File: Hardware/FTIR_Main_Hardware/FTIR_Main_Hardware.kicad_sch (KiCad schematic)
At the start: 78 parts, among them J1 RJ45_LED_Shielded, Q1 IRF7606PBF, Q2 BSS138, Q3 IRF7606PBF, Q4 BSS138, Q5 IRF7606PBF, Q6 BSS138, U1 Opamp_Dual, U2 TMC2208, U3 OKI, U6 Peensy4.1_DEV-16771, U7 OKI

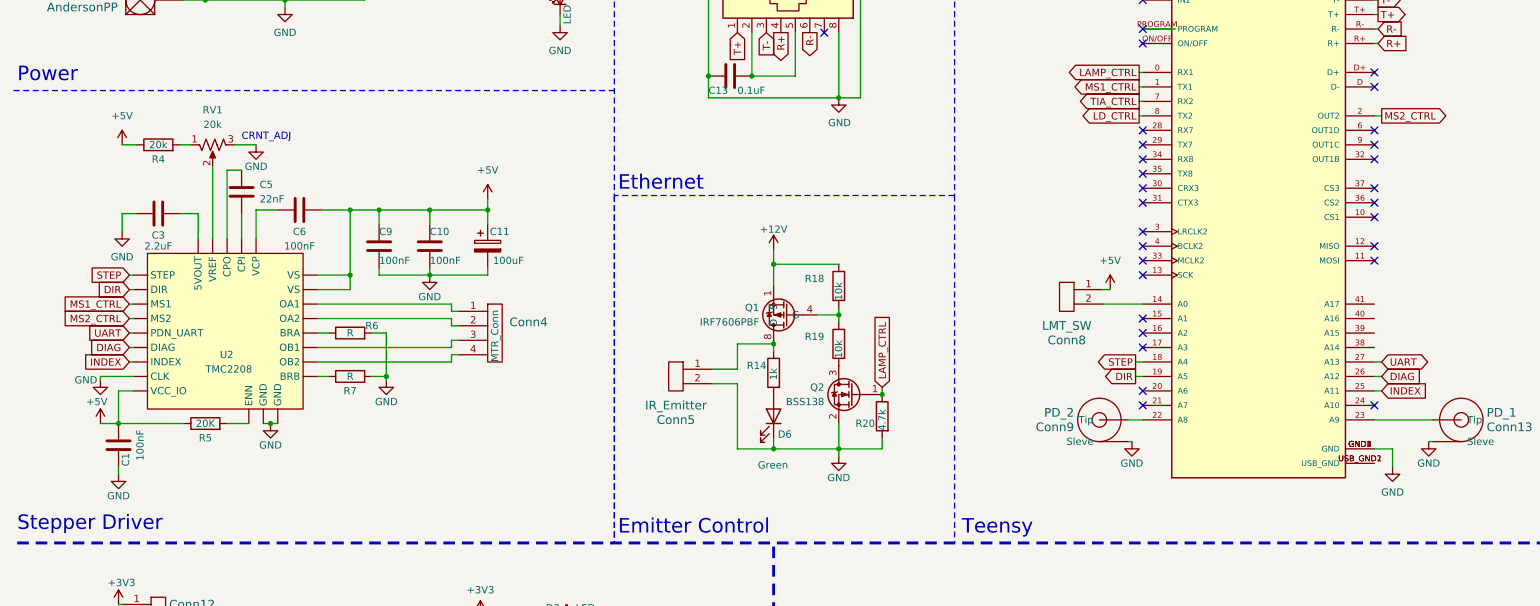
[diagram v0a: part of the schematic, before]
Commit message: Added breakouts
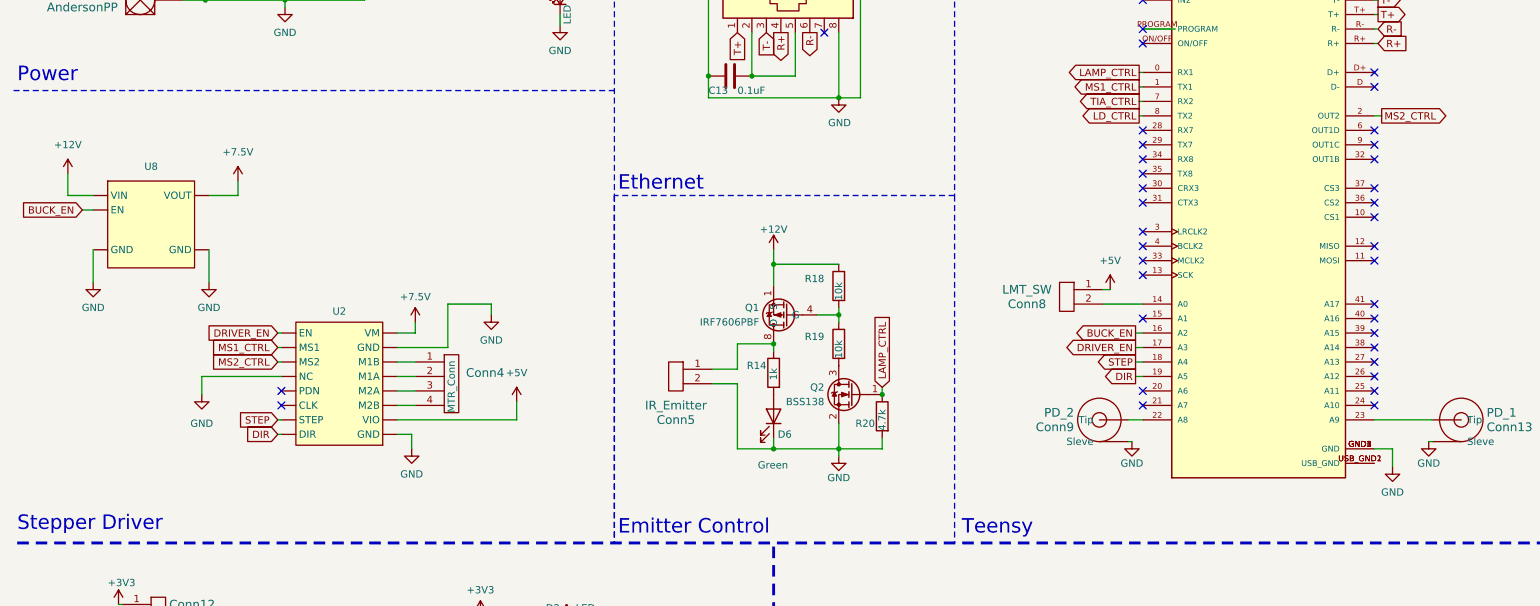
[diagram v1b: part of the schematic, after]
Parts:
- removed C1, C10, C6, C9: 100nF, symbol Device:C
- removed C11: 100uF, symbol Device:C_Polarized
- removed C3: 2.2uF, symbol Device:C
- removed C5: 22nF, symbol Device:C
- removed R4: 20k, symbol Device:R
- removed R5: 20K, symbol Device:R
- removed R6, R7: R, symbol Device:R
- removed RV1: 20k, symbol Device:R_Potentiometer_US
- removed U2: TMC2208, symbol MRDT_Devices:TMC2208
- added U2: ~, symbol Stepper_Driver_Headers:TMC2208_Breakout
- added U8: ~, symbol Stepper_Driver_Headers:Pololu_7v5_Stepdown
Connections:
- net +12V: now also U8. (VOUT)
- net +5V: now also U2. (VM)
- net DIR: now also U2. (VM)
- net GND: now also U2. (VM), U8. (VOUT)
- net MS1_CTRL: now also U2. (VM)
- net MS2_CTRL: now also U2. (VM)
- net STEP: now also U2. (VM)
- net at Conn4.1: now also U2. (VM)
- net at Conn4.2: now also U2. (VM)
- net at Conn4.3: now also U2. (VM)
- net at Conn4.4: now also U2. (VM)
- net BUCK_EN: now reaches U6.16 (A2)
- net BUCK_EN: now also U8. (VOUT)
- net DRIVER_EN: now reaches U6.17 (A3)
- net DRIVER_EN: now also U2. (VM)
- net DIAG: no longer names the net of U6.26 (A12)
- net INDEX: no longer names the net of U6.25 (A11)
- net UART: no longer names the net of U6.27 (A13)
- new net +7.5V: U2. (VM), U8. (VOUT)
- no-connect marks 37 -> 44
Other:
- note removed: "CRNT_ADJ"
- moved on the sheet: Conn4

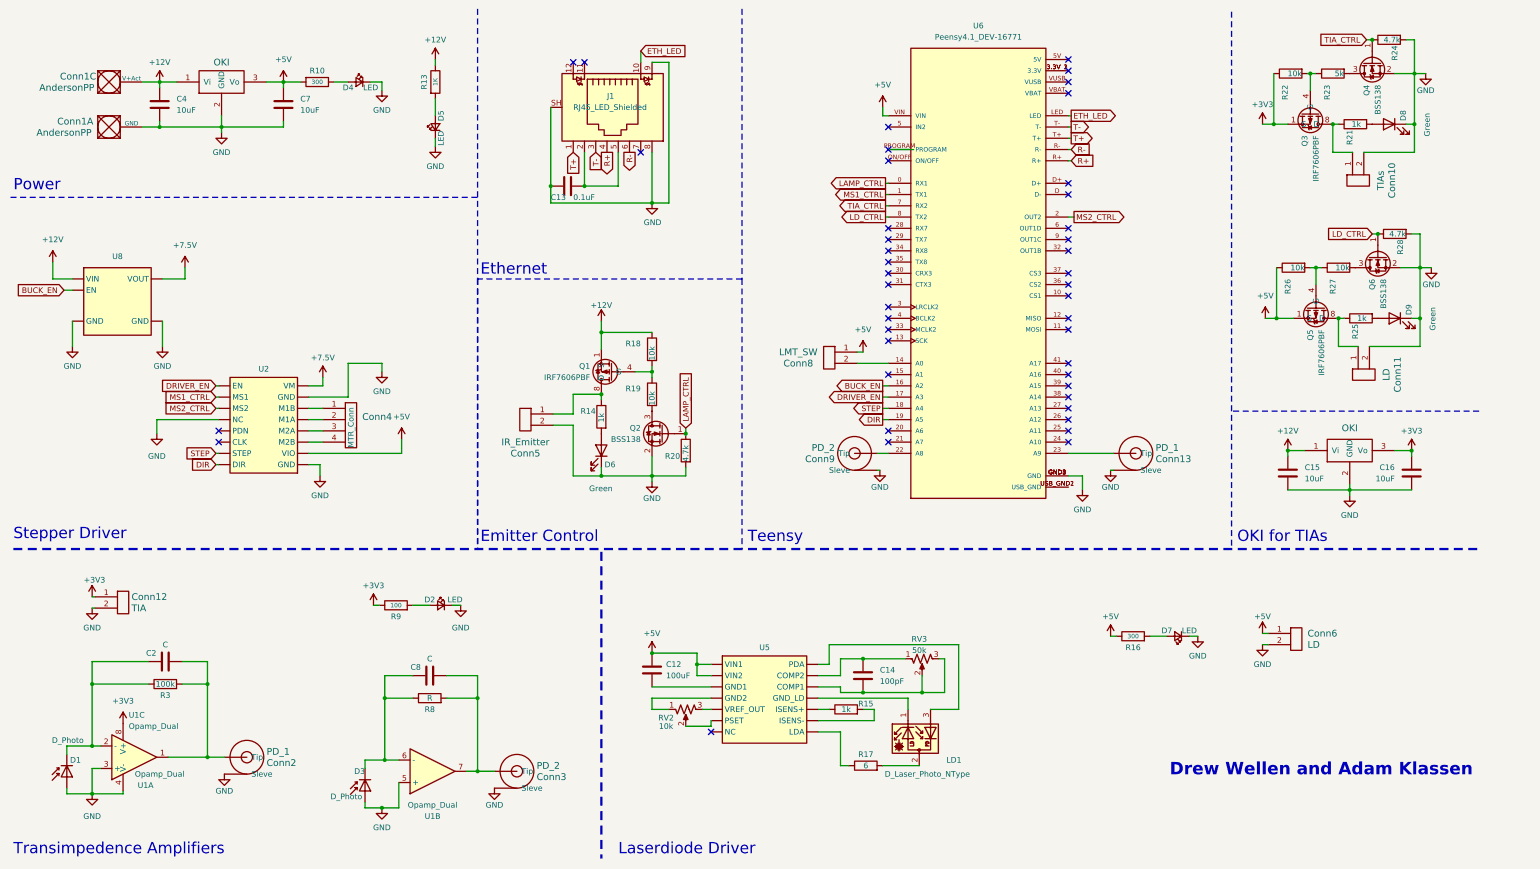
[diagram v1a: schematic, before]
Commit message: Removed more stuff
thanks, Malacki
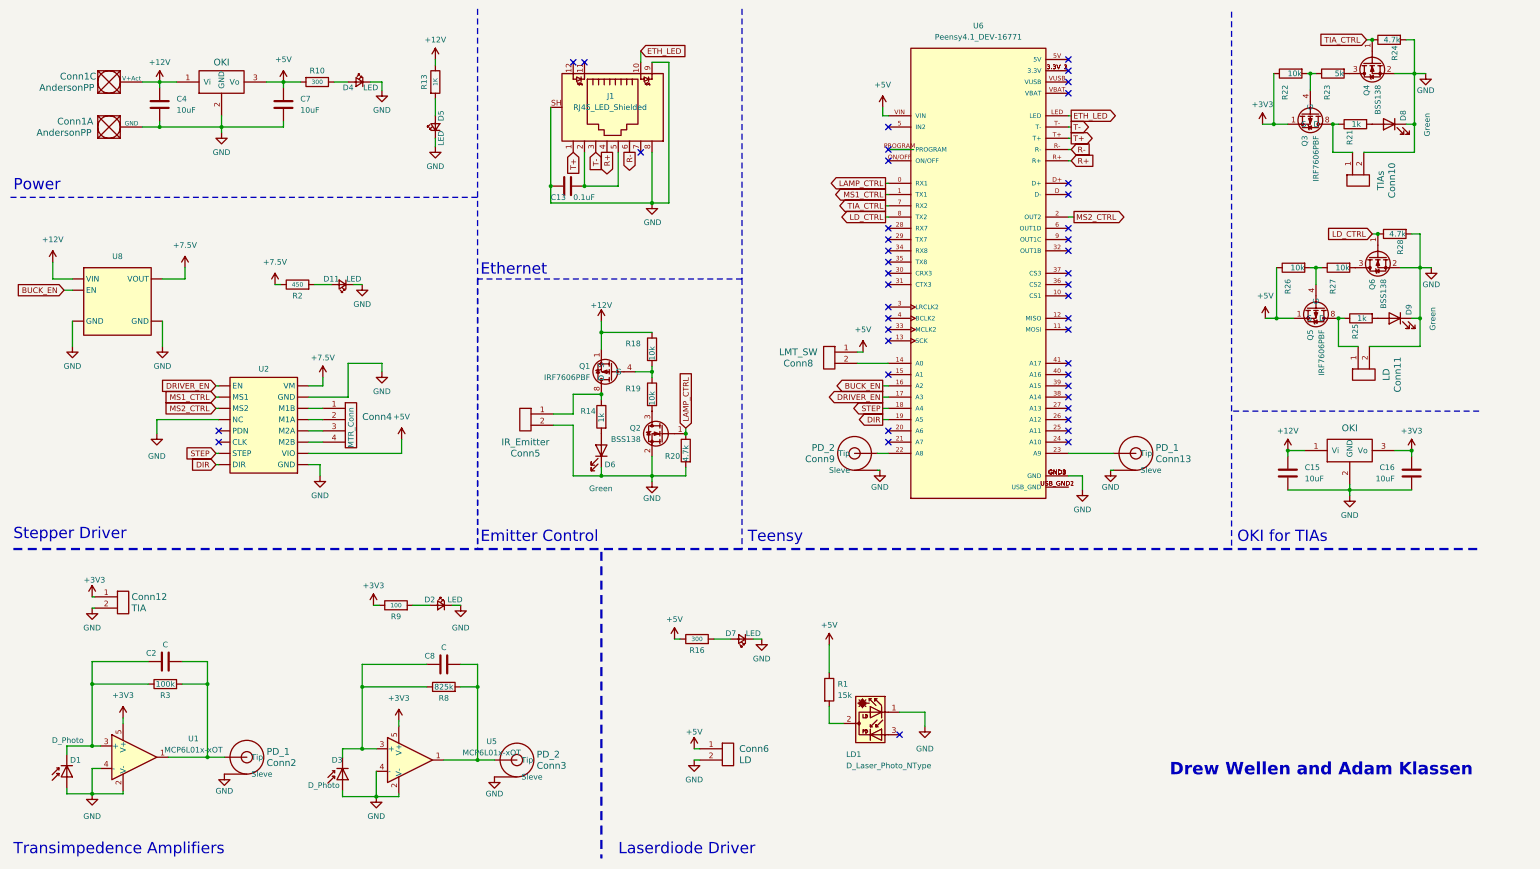
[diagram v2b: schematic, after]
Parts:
- removed C12: 100uF, symbol Device:C
- removed C14: 100pF, symbol Device:C
- removed R15: 1k, symbol Device:R
- removed R17: 6, symbol Device:R
- removed RV2: 10k, symbol Device:R_Potentiometer_US
- removed RV3: 50k, symbol Device:R_Potentiometer_US
- removed U1: Opamp_Dual, symbol Device:Opamp_Dual
- removed U5: ~, symbol MRDT_Devices:MLD203P2
- added D11: LED, LED_SMD:LED_0603_1608Metric_Pad1.05x0.95mm_HandSolder, symbol Device:LED_Small
- added R1: 15k, symbol Device:R
- added R2: 450, Resistor_SMD:R_0603_1608Metric_Pad0.98x0.95mm_HandSolder, symbol Device:R
- added U1, U5: MCP6L01x-xOT, Package_TO_SOT_SMD:SOT-23-5, symbol Amplifier_Operational:MCP6L01x-xOT
- R8: value R -> 825k
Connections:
- net +3V3: now also U1.5 (V+), U5.5 (V+)
- net +5V: now also R1.1
- net +7.5V: now also R2.1
- net GND: now also LD1.1, D11.1 (K), U1.2 (V-), U1.4 (-), U5.2 (V-), U5.4 (-)
- net at C2.1, D1.1 (K), R3.1: now also U1.3 (+)
- net at C2.2, Conn2.1 (Tip), R3.2: now also U1.1
- net at C8.1, D3.1 (K), R8.1: now also U5.3 (+)
- net at LD1.2: now also R1.2
- net at C8.2, Conn3.1 (Tip), R8.2: now also U5.1
- new net: D11.2 (A), R2.2
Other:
- moved on the sheet: C8, Conn3, Conn6, D3, D7, LD1, R16, R8

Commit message: Starting BOM
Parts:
- J1: Description  On BMS Box -> (none)
- U6: value Peensy4.1_DEV-16771 -> Teensy4.1_DEV-16771
- renumbered C4 to C1, C7 to C3, C8 to C4, C13 to C5, C15 to C6, C16 to C7, Conn13 to Conn10, Conn10 to Conn11, Conn11 to Conn12, Conn12 to Conn2, Conn2 to Conn3, Conn3 to Conn5, Conn5 to Conn6, Conn6 to Conn7, D9 to D10, D11 to D2, D2 to D6, D6 to D7, D7 to D8, D8 to D9, Q5 to Q4, Q4 to Q5, R3 to R1, R20 to R10, R16 to R11, R1 to R12, R22 to R13, R26 to R14, R23 to R15, R27 to R16, R21 to R17, R25 to R18, R24 to R19, R28 to R20, R10 to R3, R9 to R4, R13 to R5, R8 to R6, R14 to R7, R18 to R8, R19 to R9, U8 to U2, U2 to U4
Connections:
- net +12V: now also Conn1.2 (V+Log); no longer Conn1.3 (V+Act)
- net +3V3: now also Conn8.1
- net +5V: no longer Conn8.1
- net GND: now also U6.USB_GND1 (USB_GND), U6.USB_GND2 (USB_GND)
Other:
- note added: "Laserdiode Board"
- note added: "Transimpedence Amplifiers (TIAs)"
- note removed: "Laserdiode Driver"
- note removed: "Transimpedence Amplifiers"
- moved on the sheet: Conn4, R12, U2, U4
